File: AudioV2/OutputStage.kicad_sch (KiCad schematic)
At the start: 6 parts, among them SW101 DEST L (PHONE/MUTE/LINE), SW102 DEST R (PHONE/MUTE/LINE)

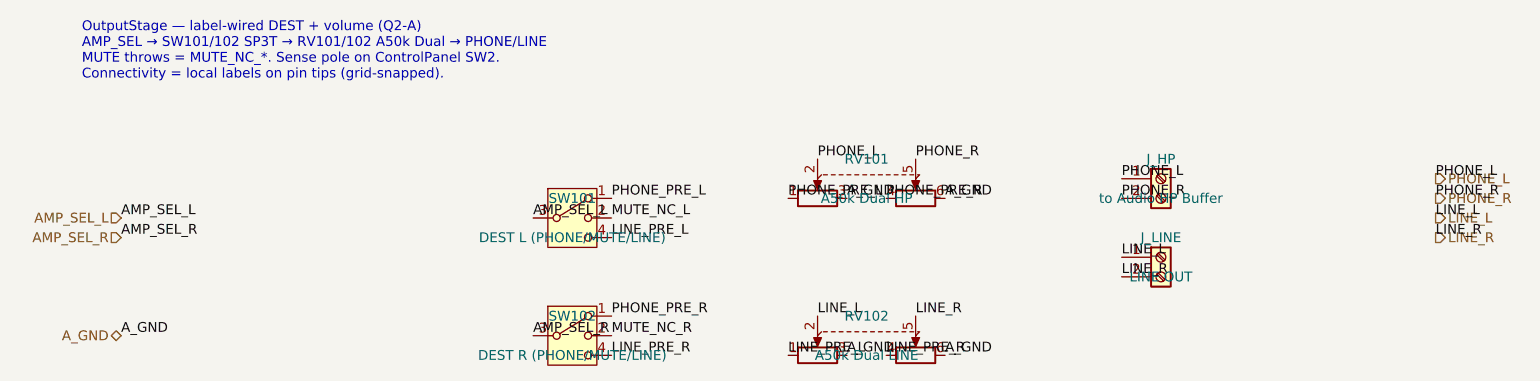
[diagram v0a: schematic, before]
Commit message: AudioV2: Power PD端子整理とエージェント引き継ぎ更新
PowerModule に J201/J202/J203 を揃え、PWR SW は ControlPanel に戻す。
AGENT_HANDOFF / WIRING に現状トポロジと PD A/B メモを残し、クラウド同期用に main へ載せる。

Co-authored-by: Cursor <cursoragent@cursor.com>
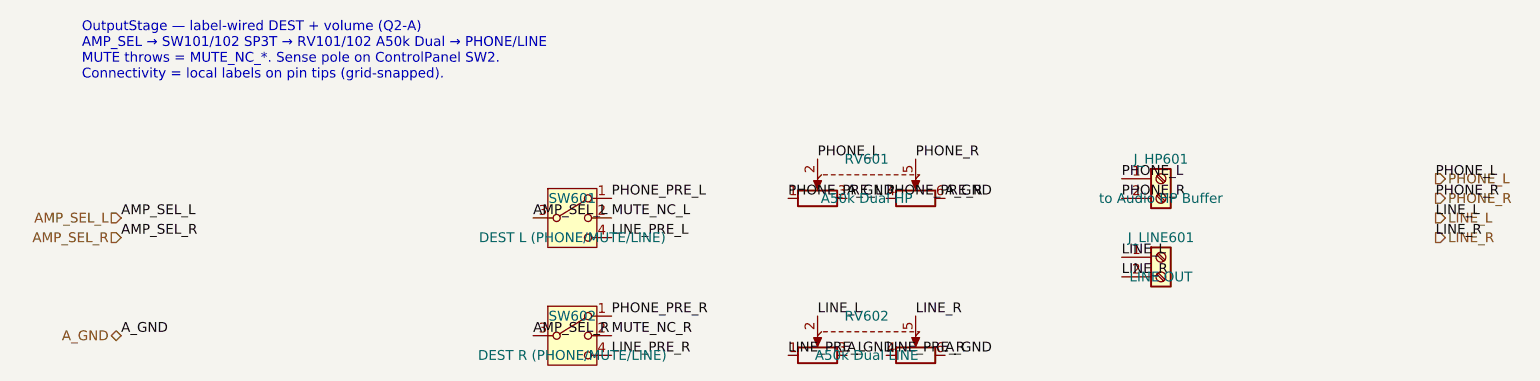
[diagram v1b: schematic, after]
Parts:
- renumbered J_HP to J_HP601, J_LINE to J_LINE601, RV101 to RV601, RV102 to RV602, SW101 to SW601, SW102 to SW602
